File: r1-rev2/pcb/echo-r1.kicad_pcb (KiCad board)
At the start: 6 copper layers, 90.8 x 100.6 mm, 79 parts, among them J1 TYPE-C-31-M-12, J2 TF-115, J3 HP_3.5mm, J4 LO_3.5mm, J6 AFC07-S30ECA-00, SW1 A, SW10 SELECT, SW11 VOL+, SW12 VOL-, SW13 POWER, SW14 HOLD, SW2 B, SW3 X, SW4 Y, SW5 DPAD↑, SW6 DPAD↓, SW7 DPAD←, SW8 DPAD→, SW9 START, U1 STM32H7R3Z8Jx, U2 W958D8NBYA5I, U3 TLV320AIC3104, Y1 SC-32S32.768kHz20PPM12.5pF, Y2 XTM32024000JT00351001

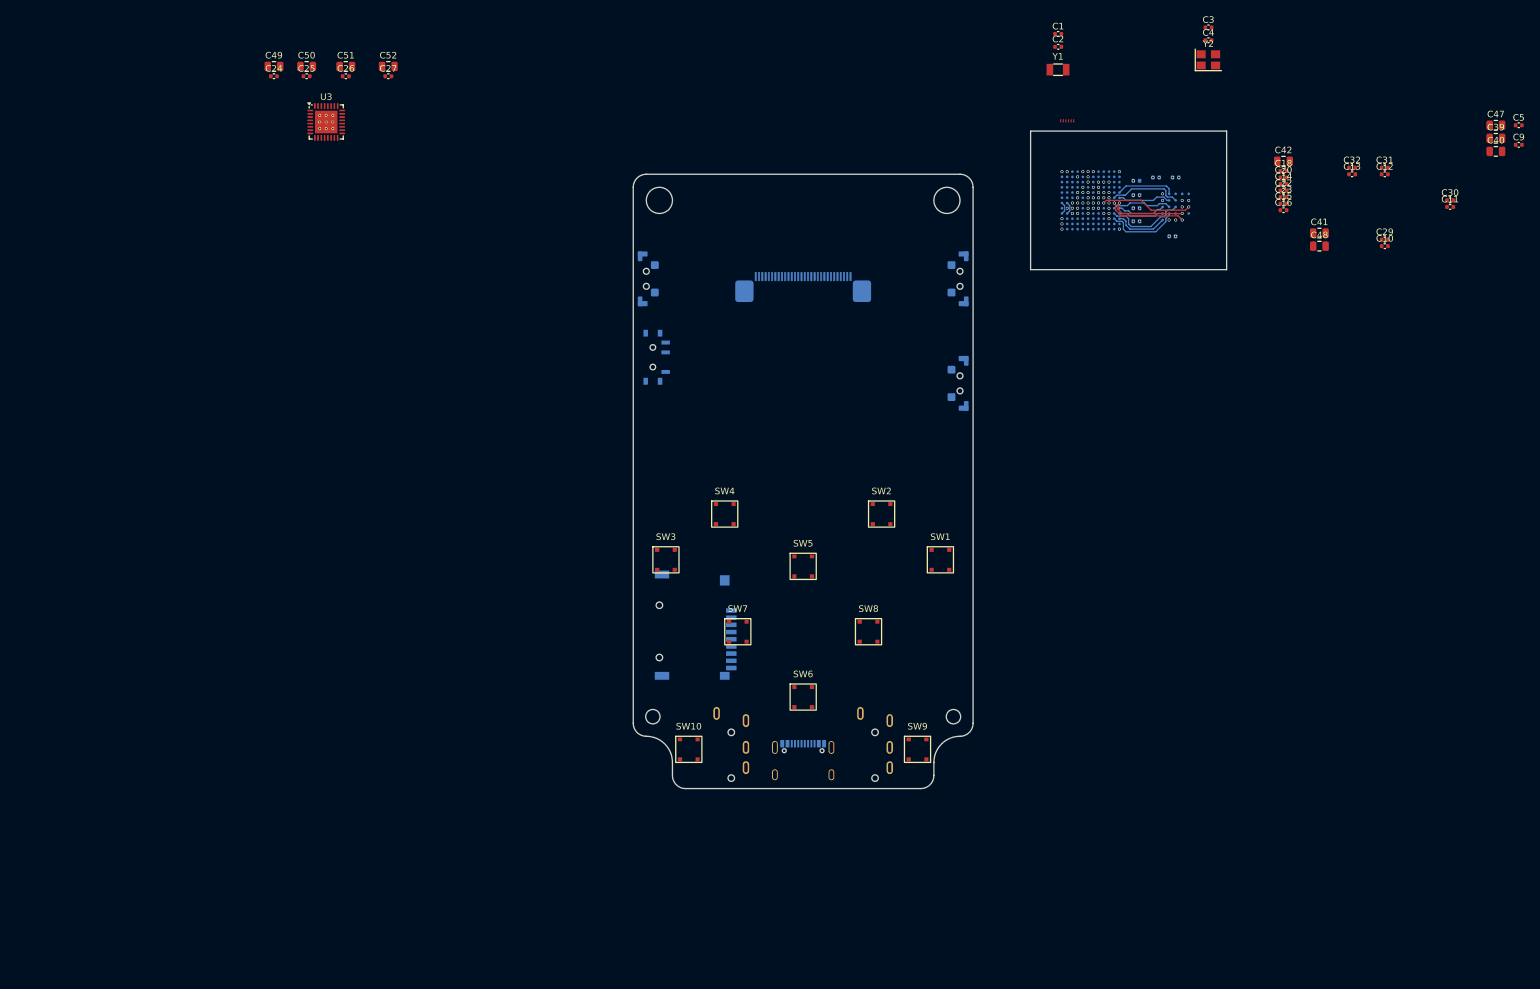
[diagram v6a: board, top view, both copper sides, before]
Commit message: R1-Rev2: add inductor footprint and group components
Also use the same 2.2uH inductor for the buck converters,
to minimize unique component count.
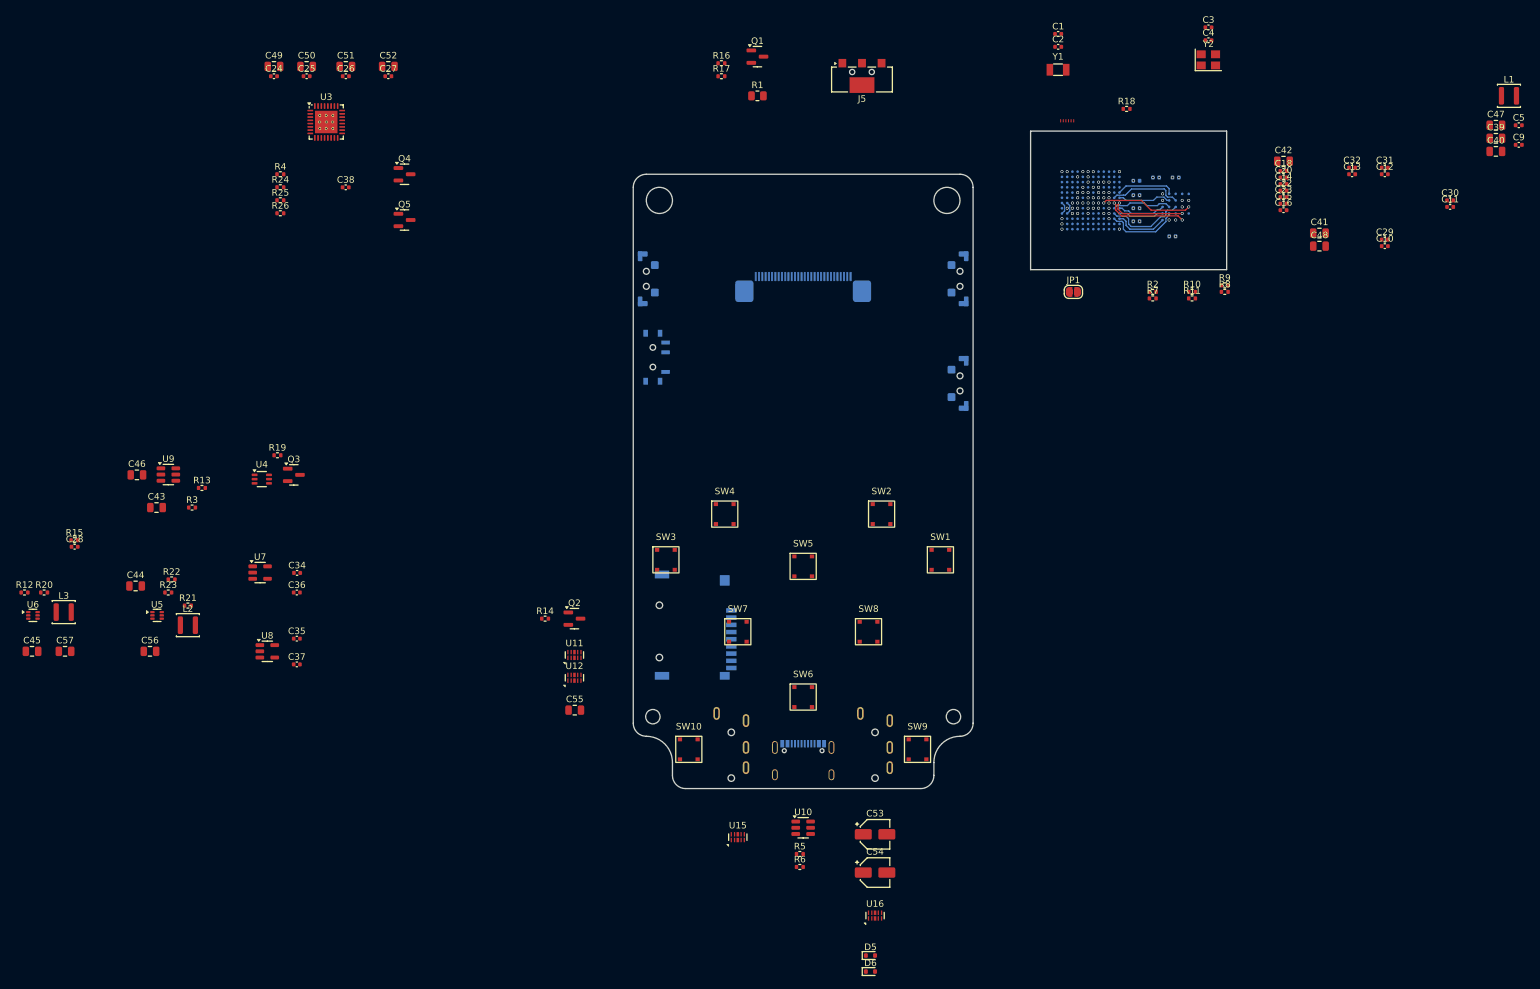
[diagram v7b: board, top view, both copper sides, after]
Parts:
- added C28: 1 µF, Capacitor_SMD:C_0402_1005Metric, F.Cu at (36.0, 115.0)
- added C34: 1 µF, Capacitor_SMD:C_0402_1005Metric, F.Cu at (70.1, 119.0)
- added C35: 1 µF, Capacitor_SMD:C_0402_1005Metric, F.Cu at (70.0, 129.1)
- added C36: 1 µF, Capacitor_SMD:C_0402_1005Metric, F.Cu at (70.0, 122.0)
- added C37: 1 µF, Capacitor_SMD:C_0402_1005Metric, F.Cu at (70.0, 133.0)
- added C38: 1 µF, Capacitor_SMD:C_0402_1005Metric, F.Cu at (77.5, 60.0)
- added C43: 4.7 µF, Capacitor_SMD:C_0805_2012Metric, F.Cu at (48.5, 109.0)
- added C44: 4.7 µF, Capacitor_SMD:C_0805_2012Metric, F.Cu at (45.4, 121.0)
- added C45: 4.7 µF, Capacitor_SMD:C_0805_2012Metric, F.Cu at (29.5, 131.0)
- added C46: 4.7 µF, Capacitor_SMD:C_0805_2012Metric, F.Cu at (45.5, 104.0)
- added C53: 10 µF/Al, Capacitor_SMD:CP_Elec_4x5.4, F.Cu at (158.5, 159.0)
- added C54: 10 µF/Al, Capacitor_SMD:CP_Elec_4x5.4, F.Cu at (158.5, 164.8)
- added C55: 22 µF, Capacitor_SMD:C_0805_2012Metric, F.Cu at (112.5, 140.0)
- added C56: 22 µF, Capacitor_SMD:C_0805_2012Metric, F.Cu at (47.5, 131.0)
- added C57: 22 µF, Capacitor_SMD:C_0805_2012Metric, F.Cu at (34.5, 131.0)
- added D5: ESD5Z3.3C, Diode_SMD:D_SOD-523, F.Cu at (157.8, 177.6)
- added D6: ESD5Z3.3C, Diode_SMD:D_SOD-523, F.Cu at (157.8, 180.0)
- added J5: GT-BTP30003-xxxA-16A, echoplayer:Conn_GT-BTP30003-xxxxA-016A, F.Cu at (156.5, 42.4)
- added JP1: SolderJumper_2_Open, Jumper:SolderJumper-2_P1.3mm_Open_RoundedPad1.0x1.5mm, F.Cu at (188.8, 76.0)
- added L1: 2.2 µH, Inductor_SMD:L_Changjiang_FNR3015S, F.Cu at (255.5, 46.0)
- added L2: 2.2 µH, Inductor_SMD:L_Changjiang_FNR3015S, F.Cu at (53.4, 127.0)
- added L3: 2.2 µH, Inductor_SMD:L_Changjiang_FNR3015S, F.Cu at (34.4, 125.0)
- added Q1: AO3401A, Package_TO_SOT_SMD:SOT-23, F.Cu at (140.5, 40.0)
- added Q2: AO3401A, Package_TO_SOT_SMD:SOT-23, F.Cu at (112.5, 126.0)
- added Q3: AO3401A, Package_TO_SOT_SMD:SOT-23, F.Cu at (69.6, 104.0)
- added Q4: AO3401A, Package_TO_SOT_SMD:SOT-23, F.Cu at (86.5, 58.0)
- added Q5: AO3401A, Package_TO_SOT_SMD:SOT-23, F.Cu at (86.5, 65.0)
- added R1: 3.9 Ω, 125 mW, Resistor_SMD:R_0805_2012Metric, F.Cu at (140.5, 46.0)
- added R10: 15 kΩ, Resistor_SMD:R_0402_1005Metric, F.Cu at (207.0, 76.0)
- added R11: 15 kΩ, Resistor_SMD:R_0402_1005Metric, F.Cu at (207.0, 77.0)
- added R12: 15 kΩ, Resistor_SMD:R_0402_1005Metric, F.Cu at (28.4, 122.0)
- added R13: 15 kΩ, Resistor_SMD:R_0402_1005Metric, F.Cu at (55.5, 106.0)
- added R14: 68 kΩ, Resistor_SMD:R_0402_1005Metric, F.Cu at (108.0, 126.0)
- added R15: 68 kΩ, Resistor_SMD:R_0402_1005Metric, F.Cu at (36.0, 114.0)
- added R16: 68 kΩ, Resistor_SMD:R_0402_1005Metric, F.Cu at (135.0, 41.0)
- added R17: 68 kΩ, Resistor_SMD:R_0402_1005Metric, F.Cu at (135.0, 43.0)
- added R18: 68 kΩ, Resistor_SMD:R_0402_1005Metric, F.Cu at (197.0, 48.0)
- added R19: 68 kΩ, Resistor_SMD:R_0402_1005Metric, F.Cu at (67.1, 101.0)
- added R2: 2.2 kΩ, Resistor_SMD:R_0402_1005Metric, F.Cu at (201.0, 76.0)
- added R20: 68 kΩ, Resistor_SMD:R_0402_1005Metric, F.Cu at (31.4, 122.0)
- added R21: 68 kΩ, Resistor_SMD:R_0402_1005Metric, F.Cu at (53.4, 124.0)
- added R22: 68 kΩ, Resistor_SMD:R_0402_1005Metric, F.Cu at (50.9, 120.0)
- added R23: 68 kΩ, Resistor_SMD:R_0402_1005Metric, F.Cu at (50.4, 122.0)
- added R24: 68 kΩ, Resistor_SMD:R_0402_1005Metric, F.Cu at (67.5, 60.0)
- added R25: 68 kΩ, Resistor_SMD:R_0402_1005Metric, F.Cu at (67.5, 62.0)
- added R26: 68 kΩ, Resistor_SMD:R_0402_1005Metric, F.Cu at (67.5, 64.0)
- added R3: 2.2 kΩ, Resistor_SMD:R_0402_1005Metric, F.Cu at (54.0, 109.0)
- added R4: 2.2 kΩ, Resistor_SMD:R_0402_1005Metric, F.Cu at (67.5, 58.0)
- added R5: 5.1 kΩ, Resistor_SMD:R_0402_1005Metric, F.Cu at (147.0, 162.0)
- added R6: 5.1 kΩ, Resistor_SMD:R_0402_1005Metric, F.Cu at (147.0, 164.0)
- added R7: 5.1 kΩ, Resistor_SMD:R_0402_1005Metric, F.Cu at (201.0, 77.0)
- added R8: 15 kΩ, Resistor_SMD:R_0402_1005Metric, F.Cu at (212.0, 76.0)
- added R9: 15 kΩ, Resistor_SMD:R_0402_1005Metric, F.Cu at (212.0, 75.0)
- added U10: USBLC6-2SC6, Package_TO_SOT_SMD:SOT-23-6, F.Cu at (147.5, 158.0)
- added U11: TPAZ1143-04F, echoplayer:TECHPUBLIC_UDFN-10_1.0x2.5mm_P0.5mm, F.Cu at (112.5, 131.6)
- added U12: TPAZ1143-04F, echoplayer:TECHPUBLIC_UDFN-10_1.0x2.5mm_P0.5mm, F.Cu at (112.5, 135.0)
- added U15: TPAZ1143-04F, echoplayer:TECHPUBLIC_UDFN-10_1.0x2.5mm_P0.5mm, F.Cu at (137.5, 159.4)
- added U16: TPAZ1143-04F, echoplayer:TECHPUBLIC_UDFN-10_1.0x2.5mm_P0.5mm, F.Cu at (158.5, 171.4)
- added U4: LM66100DCK, Package_TO_SOT_SMD:Texas_R-PDSO-G6, F.Cu at (64.7, 104.7)
- added U5: TPS62A01DRLR, Package_TO_SOT_SMD:SOT-563, F.Cu at (48.6, 125.5)
- added U6: TPS62A01DRLR, Package_TO_SOT_SMD:SOT-563, F.Cu at (29.6, 125.5)
- added U7: AP2125K-3.0, Package_TO_SOT_SMD:SOT-23-5, F.Cu at (64.4, 119.0)
- added U8: AP2125K-3.0, Package_TO_SOT_SMD:SOT-23-5, F.Cu at (65.5, 131.0)
- added U9: TP4057, Package_TO_SOT_SMD:TSOT-23-6, F.Cu at (50.4, 104.0)

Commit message: R1-Rev2: improve reset circuit, add XSPI CS pullup
Connect NRST to xspi_reset and the regulator power-good signals.
This should ensure that the STM32 and RAM will stay in reset
until both power rails have started up. It shouldn't be necessary
to control xspi_reset with a GPIO, but for now leave it connected
just in case.

The XSPI CS pin also requires an external pullup to guarantee it
will be pulled high during power-on, which is required to ensure
the RAM resets properly.
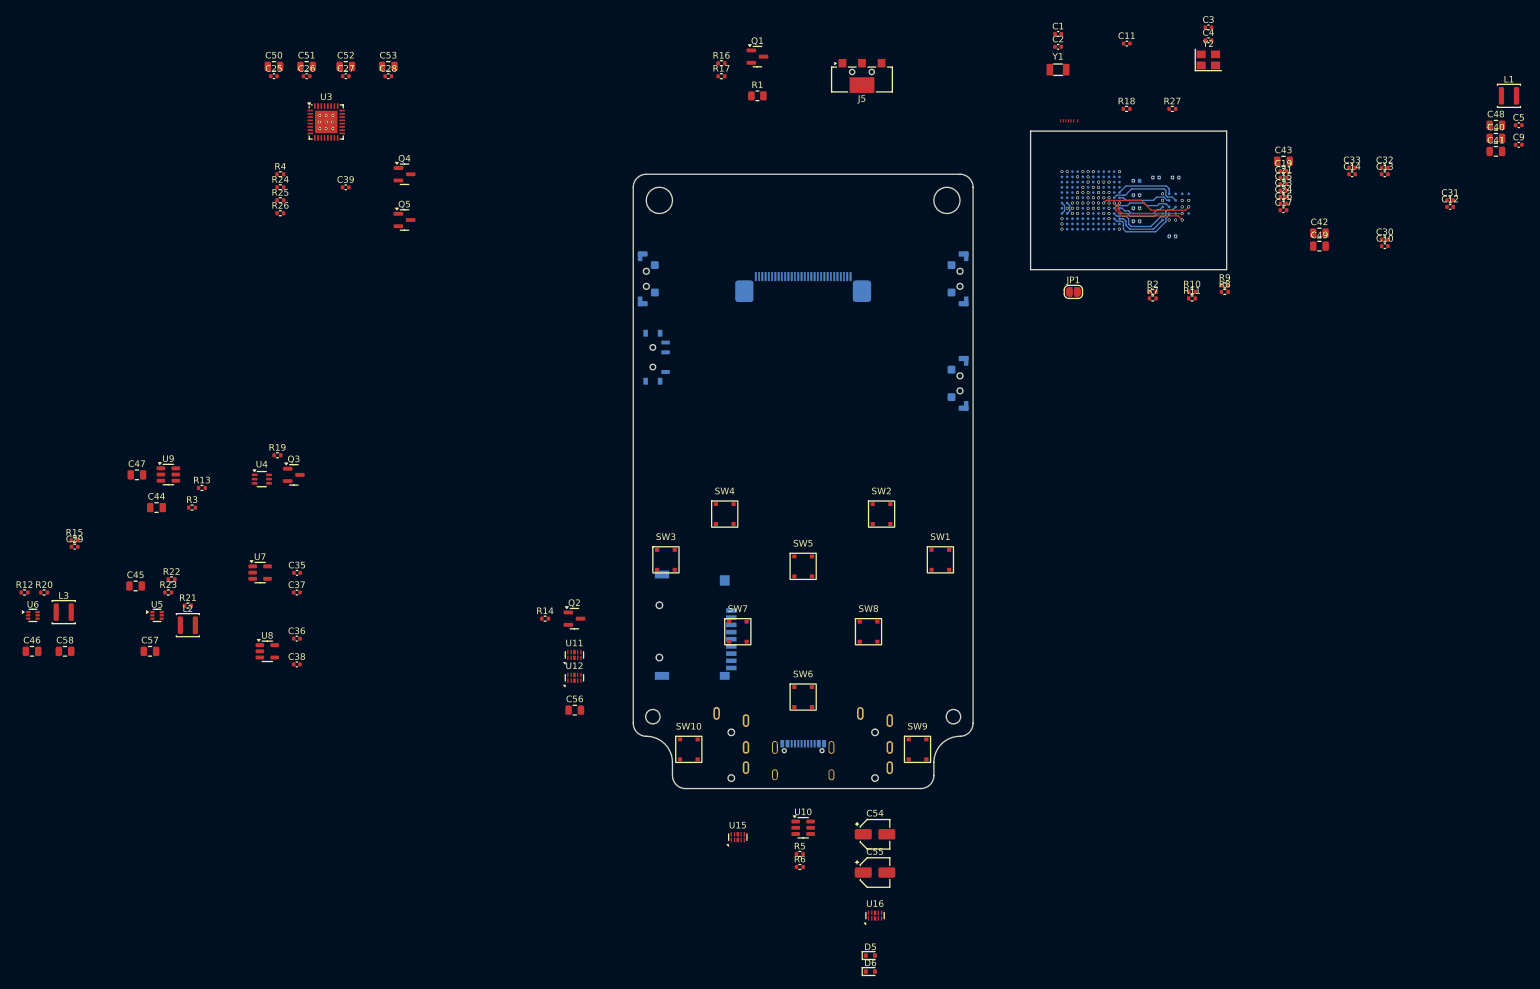
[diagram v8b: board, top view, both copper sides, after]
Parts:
- added C11: 100 nF, Capacitor_SMD:C_0402_1005Metric, F.Cu at (197.0, 38.0)
- added NT11: NetTie_2, echoplayer:NetTie_0.15mm_SMD, F.Cu at (189.5, 49.8)
- added R27: 68 kΩ, Resistor_SMD:R_0402_1005Metric, F.Cu at (204.0, 48.0)
- renumbered C11 to C12, C12 to C13, C13 to C14, C14 to C15, C15 to C16, C16 to C17, C17 to C18, C18 to C19, C19 to C20, C20 to C21, C21 to C22, C22 to C23, C23 to C24, C24 to C25, C25 to C26, C26 to C27, C27 to C28, C28 to C29, C29 to C30, C30 to C31, C31 to C32, C32 to C33, C33 to C34, C34 to C35, C35 to C36, C36 to C37, C37 to C38, C38 to C39, C39 to C40, C40 to C41, C41 to C42, C42 to C43, C43 to C44, C44 to C45, C45 to C46, C46 to C47, C47 to C48, C48 to C49, C49 to C50, C50 to C51, C51 to C52, C52 to C53, C53 to C54, C54 to C55, C55 to C56, C56 to C57, C57 to C58
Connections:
- U5 pad 6: GND -> /swd.nrst
- U6 pad 6: GND -> /swd.nrst
